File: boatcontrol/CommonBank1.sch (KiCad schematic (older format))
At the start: 21 parts, among them J201 Conn_01x01_Male, J202 Conn_01x01_Male, J203 TBP01R2W-508-16BE, J204 Conn_01x01_Male, J205 Conn_01x01_Male, J206 TBL008V-1000-02BE, Q203 IRF9510PBF-BE3, U201 MCP23017-E/SP, U202 MCP23017-E/SP

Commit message: Try labels on subcharts
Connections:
- net labels added: 12C_RAW
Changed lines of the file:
@@
 L power:+12C #PWR?
 U 1 1 D1AAA2AE
-P 9000 6050
+P 8100 6050
 AR Path="/D1AAA2AE" Ref="#PWR?"  Part="1"
 AR Path="/D16552B4/D1AAA2AE" Ref="#PWR0205"  Part="1"
 AR Path="/D1BB8DB4/D1AAA2AE" Ref="#PWR?"  Part="1"
-F 0 "#PWR0205" H 9000 5900 50  0001 C CNN
-F 1 "+12C" H 8950 6200 50  0000 L CNN
-F 2 "" H 9000 6050 50  0001 C CNN
-F 3 "" H 9000 6050 50  0001 C CNN
-	1    9000 6050
+F 0 "#PWR0205" H 8100 5900 50  0001 C CNN
+F 1 "+12C" H 8050 6200 50  0000 L CNN
+F 2 "" H 8100 6050 50  0001 C CNN
+F 3 "" H 8100 6050 50  0001 C CNN
+	1    8100 6050
 	1    0    0    -1
 $EndComp
@@
 Wire Wire Line
 	6700 4600 7550 4600
-Wire Wire Line
-	9250 6050 9000 6050
 Wire Wire Line
 	6750 1050 6700 1050
@@
 L power:PWR_FLAG #FLG0201
 U 1 1 5F1AB3C0
-P 9250 6050
-F 0 "#FLG0201" H 9250 6125 50  0001 C CNN
-F 1 "PWR_FLAG" H 9250 6223 50  0000 C CNN
-F 2 "" H 9250 6050 50  0001 C CNN
-F 3 "~" H 9250 6050 50  0001 C CNN
-	1    9250 6050
+P 8100 6050
+F 0 "#FLG0201" H 8100 6125 50  0001 C CNN
+F 1 "PWR_FLAG" H 8100 6223 50  0000 C CNN
+F 2 "" H 8100 6050 50  0001 C CNN
+F 3 "~" H 8100 6050 50  0001 C CNN
+	1    8100 6050
 	-1   0    0    1
 $EndComp
-Connection ~ 9250 6050
 Text Notes 3300 2100 3    50   ~ 0
 I2C Address 0x20
@@
 	6750 5250 6750 6050
 Wire Wire Line
-	8300 6050 6750 6050
+	8300 6050 8100 6050
 Connection ~ 6750 6050
 Wire Wire Line
 	6750 6050 6750 6250
-Wire Wire Line
-	8700 6050 9000 6050
-Connection ~ 9000 6050
 $Comp
 L power:GND #PWR0204
@@
 Wire Wire Line
 	8500 5750 8800 5750
+Text Label 9150 6050 2    50   ~ 0
+12C_RAW
+Wire Wire Line
+	8700 6050 9250 6050
+Connection ~ 8100 6050
+Wire Wire Line
+	6750 6050 8100 6050
 $EndSCHEMATC

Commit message: Bottom done
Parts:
- removed Q203: IRF9510PBF-BE3, Package_TO_SOT_THT:TO-220-3_Vertical, symbol BoatControl:IPP_B_I80P03
- added Q203: IPP120P04P4L-03, Package_TO_SOT_THT:TO-220-3_Vertical, symbol BoatControl:IPP120P04P4L-03
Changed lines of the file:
@@
 Wire Wire Line
 	1100 7150 1700 7150
-$Comp
-L BoatControl:IPP_B_I80P03 Q?
-U 1 1 6232FD99
-P 8500 6050
-AR Path="/6232FD99" Ref="Q?"  Part="1"
-AR Path="/D16552B4/6232FD99" Ref="Q203"  Part="1"
-F 0 "Q203" V 8350 5850 50  0000 L CNN
-F 1 "IRF9510PBF-BE3" V 8750 5850 50  0000 L CNN
-F 2 "Package_TO_SOT_THT:TO-220-3_Vertical" H 8500 6050 50  0001 C CNN
-F 3 "https://www.vishay.com/docs/91072/91072.pdf" H 8500 6050 50  0001 C CNN
-F 4 "P-Channel 100V 4A (Tc) 43W (Tc) Through Hole TO-220AB" H 8500 6050 50  0001 C CNN "Description"
-F 5 "Vishay Siliconix" H 8500 6050 50  0001 C CNN "Manufacturer"
-	1    8500 6050
-	0    1    1    0
-$EndComp
 Wire Wire Line
 	6750 5250 6750 6050
@@
 Wire Wire Line
 	6750 6050 8100 6050
+$Comp
+L BoatControl:IPP120P04P4L-03 Q203
+U 1 1 5FEBFE7C
+P 8500 6050
+F 0 "Q203" V 8150 6050 50  0000 C CNN
+F 1 "IPP120P04P4L-03" V 8650 6250 50  0000 C CNN
+F 2 "Package_TO_SOT_THT:TO-220-3_Vertical" H 8150 6600 50  0001 C CNN
+F 3 "https://www.infineon.com/dgdl/Infineon-I80P03P4L_04-DS-v01_01-en.pdf?folderId=db3a304314dca3890114ef902baa05f9&fileId=db3a30431ddc9372011e07e95eb827d7&ack=t" H 8500 6050 50  0001 C CNN
+F 4 "P-Channel 30V 80A (Tc) 137W (Tc) Through Hole PG-TO220-3-1" H 8350 6700 50  0001 C CNN "Description"
+F 5 "OptiMOS" H 9100 6350 50  0001 C CNN "Series"
+F 6 "Infineon Technologies" H 9000 6450 50  0001 C CNN "Infineon Technologies"
+	1    8500 6050
+	0    1    1    0
+$EndComp
 $EndSCHEMATC

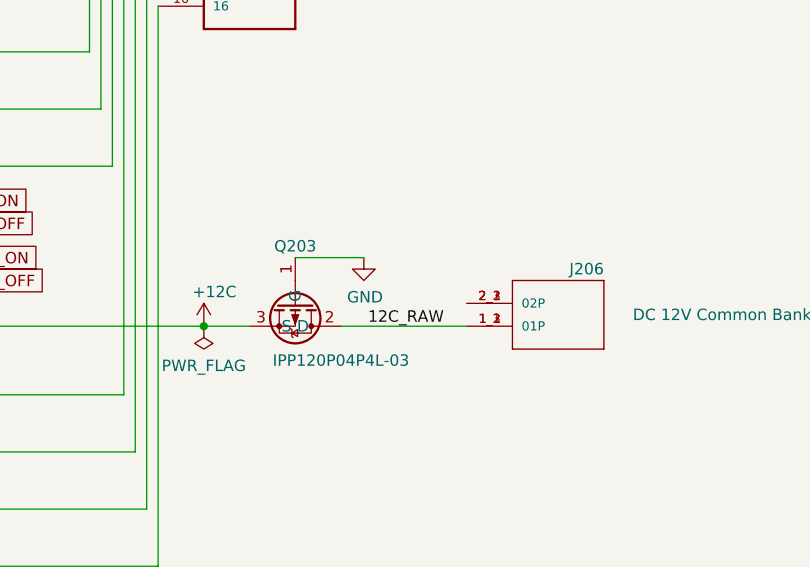
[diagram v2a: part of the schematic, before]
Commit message: Fix polarity mosfets
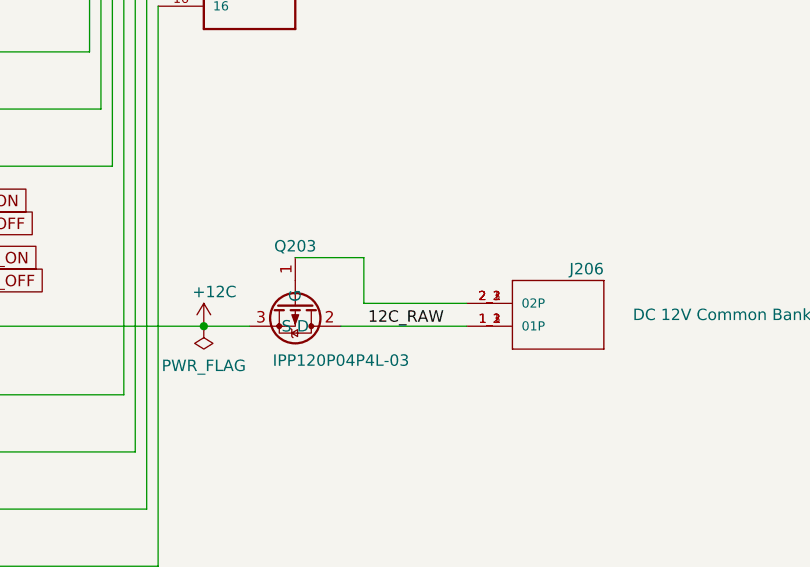
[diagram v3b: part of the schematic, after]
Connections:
- net GND: no longer Q203.1 (G)
- net at J206.2_1 (02P), J206.2_2 (02P), J206.2_3 (02P): now also Q203.1 (G)
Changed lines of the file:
@@
 Wire Wire Line
 	6750 6050 6750 6250
-$Comp
-L power:GND #PWR0204
-U 1 1 623B0B10
-P 8800 5750
-F 0 "#PWR0204" H 8800 5500 50  0001 C CNN
-F 1 "GND" H 8805 5577 50  0000 C CNN
-F 2 "" H 8800 5750 50  0001 C CNN
-F 3 "" H 8800 5750 50  0001 C CNN
-	1    8800 5750
-	1    0    0    -1
-$EndComp
 Wire Wire Line
 	4600 1650 5400 1650
@@
 	0    1    1    0
 $EndComp
+Wire Wire Line
+	9250 5950 8800 5950
+Wire Wire Line
+	8800 5950 8800 5750
 $EndSCHEMATC

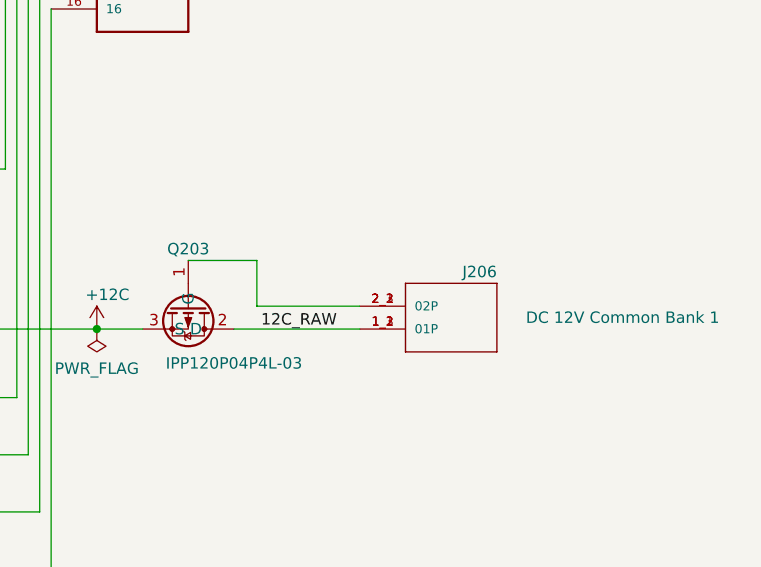
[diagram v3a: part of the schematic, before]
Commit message: Add reverse/AC/DC polarity indicators
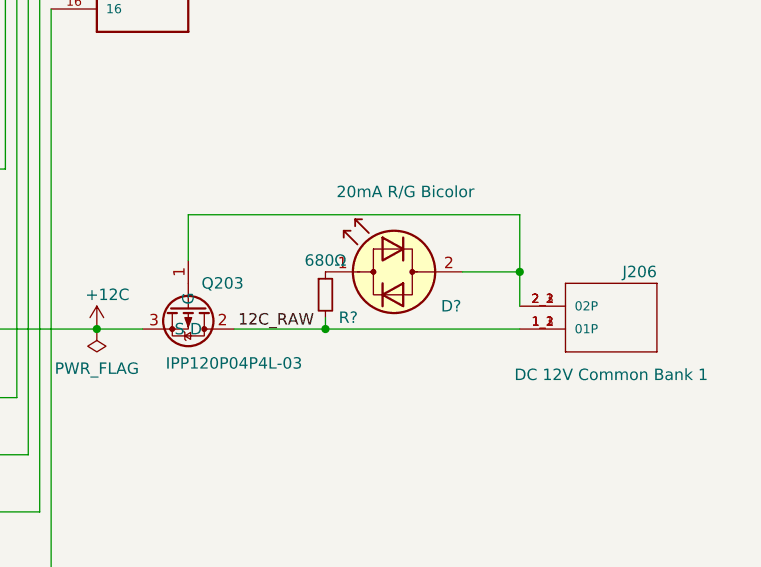
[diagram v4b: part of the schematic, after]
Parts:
- added D?: 20mA R/G Bicolor, LED_THT:LED_D5.0mm, symbol Device:LED_Dual_2pin
- added R?: 680Ω, Resistor_THT:R_Axial_DIN0207_L6.3mm_D2.5mm_P7.62mm_Horizontal, symbol Device:R_Small
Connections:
- net 12C_RAW: now also R?.2
- net at J206.2_1 (02P), J206.2_2 (02P), J206.2_3 (02P)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: now also D?.2 (AK)
- new net: D?.1 (KA), R?.1
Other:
- moved on the sheet: J206

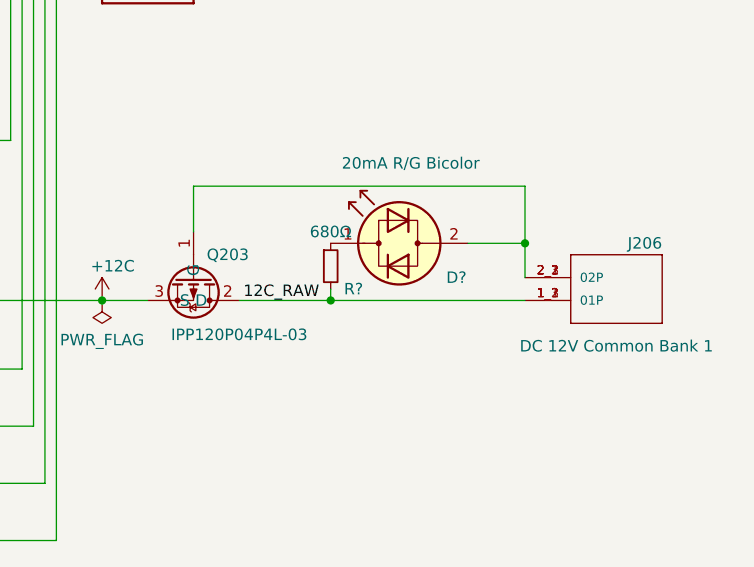
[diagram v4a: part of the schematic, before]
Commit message: Fix LED resistors
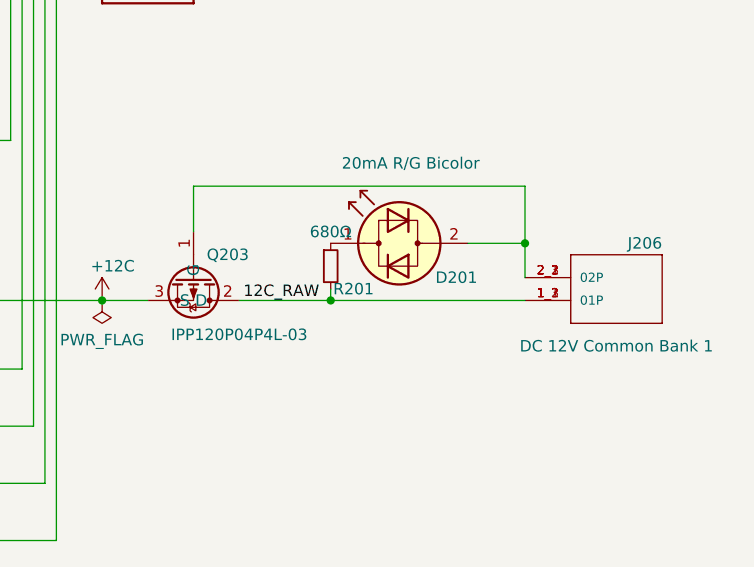
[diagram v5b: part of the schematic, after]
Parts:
- gave numbers to parts that had none: 2
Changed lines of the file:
@@
 AR Path="/D1BB8DB4/5F75E923/60474907/5FECB36F" Ref="D?"  Part="1"
 AR Path="/D1BB8DB4/5F75E923/60474911/5FECB36F" Ref="D?"  Part="1"
-AR Path="/D16552B4/5FECB36F" Ref="D?"  Part="1"
-F 0 "D?" H 9150 5650 50  0000 C CNN
+AR Path="/D16552B4/5FECB36F" Ref="D201"  Part="1"
+F 0 "D201" H 9150 5650 50  0000 C CNN
 F 1 "20mA R/G Bicolor" H 9350 6150 50  0000 C CNN
 F 2 "LED_THT:LED_D5.0mm" H 9400 5800 50  0001 C CNN
@@
 $EndComp
 $Comp
-L Device:R_Small R?
+L Device:R_Small R201
 U 1 1 5FE96CCA
 P 9100 5900
-F 0 "R?" H 9200 5800 50  0000 C CNN
+F 0 "R201" H 9200 5800 50  0000 C CNN
 F 1 "680Ω" H 9100 6050 50  0000 C CNN
 F 2 "Resistor_THT:R_Axial_DIN0207_L6.3mm_D2.5mm_P7.62mm_Horizontal" H 9100 5900 50  0001 C CNN

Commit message: Figure out wiring cluster
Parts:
- added JP209: Jumper_NO_Small, Connector_PinHeader_2.54mm:PinHeader_1x02_P2.54mm_Vertical, symbol Device:Jumper_NO_Small
- Q203: Field8 (none) -> Optional, can be substituded with shunt; Purpose (none) -> Reverse Polarity (Voltage) Protection
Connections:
- net at J206.2_1 (02P), J206.2_2 (02P), J206.2_3 (02P)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: now also JP209.1; no longer D201.2 (AK)
- new net: D201.2 (AK), JP209.2
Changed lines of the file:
@@
 F 5 "OptiMOS" H 9100 6350 50  0001 C CNN "Series"
 F 6 "Infineon Technologies" H 9000 6450 50  0001 C CNN "Infineon Technologies"
+F 7 "Reverse Polarity (Voltage) Protection" V 8800 6200 50  0000 C CNN "Purpose"
+F 8 "Optional, can be substituded with shunt" V 8900 6250 50  0000 C CNN "Field8"
 	1    8500 6050
 	0    1    1    0
@@
 Wire Wire Line
 	8500 5550 8500 5750
+$Comp
+L Device:Jumper_NO_Small JP?
+U 1 1 617F409D
+P 9800 5800
+AR Path="/617F409D" Ref="JP?"  Part="1"
+AR Path="/D16552B4/617F409D" Ref="JP209"  Part="1"
+AR Path="/D1BB8DB4/617F409D" Ref="JP?"  Part="1"
+F 0 "JP209" H 9800 5900 50  0000 C CNN
+F 1 "Jumper_NO_Small" H 9850 5700 50  0001 C CNN
+F 2 "Connector_PinHeader_2.54mm:PinHeader_1x02_P2.54mm_Vertical" H 9800 5800 50  0001 C CNN
+F 3 "~" H 9800 5800 50  0001 C CNN
+	1    9800 5800
+	-1   0    0    1
+$EndComp
 Wire Wire Line
-	9950 5800 9950 5550
+	9950 5550 9950 5800
 Wire Wire Line
-	9950 5950 9950 5800
+	9900 5800 9950 5800
 Connection ~ 9950 5800
 Wire Wire Line
-	9950 5800 9700 5800
+	9950 5800 9950 5950
 $EndSCHEMATC

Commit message: Add remaining bypass capacitors
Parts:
- C201, C203: value 10uF -> 10μF; footprint Capacitor_THT:CP_Radial_D8.0mm_P5.00mm -> Capacitor_THT:C_Disc_D7.5mm_W5.0mm_P5.00mm; symbol Device:CP1_Small -> Device:C_Small
- C202, C204: value 0.1uF -> 0.1μF; footprint Capacitor_THT:CP_Radial_D8.0mm_P5.00mm -> Capacitor_THT:C_Disc_D7.5mm_W5.0mm_P5.00mm; symbol Device:CP1_Small -> Device:C_Small
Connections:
- net 12V DC Block 3/DIG_OFF_C1: no longer U202.2 (GPB1)
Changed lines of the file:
@@
 	2350 6150 2350 4950
 Wire Wire Line
-	2350 4950 3550 4950
+	2350 4950 3200 4950
 Connection ~ 2350 6150
 Wire Wire Line
@@
 Wire Wire Line
 	2350 2000 2350 800
-Wire Wire Line
-	2350 800  3550 800
 Connection ~ 2350 2000
 Wire Wire Line
@@
 AR Path="/D1BB8DB4/5FA17E9C" Ref="#PWR?"  Part="1"
 F 0 "#PWR0203" H 3550 4800 50  0001 C CNN
-F 1 "+5V" H 3700 5000 50  0000 C CNN
+F 1 "+5V" V 3550 5150 50  0000 C CNN
 F 2 "" H 3550 4950 50  0001 C CNN
 F 3 "" H 3550 4950 50  0001 C CNN
 	1    3550 4950
-	1    0    0    -1
+	0    1    1    0
 $EndComp
 Connection ~ 3550 800
@@
 AR Path="/D1BB8DB4/5FA17EB1" Ref="#PWR?"  Part="1"
 F 0 "#PWR0201" H 3550 650 50  0001 C CNN
-F 1 "+5V" H 3700 850 50  0000 C CNN
+F 1 "+5V" V 3550 1000 50  0000 C CNN
 F 2 "" H 3550 800 50  0001 C CNN
 F 3 "" H 3550 800 50  0001 C CNN
 	1    3550 800
-	1    0    0    -1
+	0    1    1    0
 $EndComp
 Connection ~ 3550 3000
@@
 Wire Wire Line
 	5400 4600 4300 4600
-Wire Wire Line
-	4300 4600 4300 5350
 Wire Wire Line
 	5400 4750 4350 4750
@@
 	6750 6250 6750 6500
 $Comp
-L Device:CP1_Small C?
-U 1 1 61835D4A
-P 900 1800
-AR Path="/61835D4A" Ref="C?"  Part="1"
-AR Path="/D16552B4/61835D4A" Ref="C201"  Part="1"
-F 0 "C201" V 850 1550 50  0000 L CNN
-F 1 "10uF" H 991 1755 50  0001 L CNN
-F 2 "Capacitor_THT:CP_Radial_D8.0mm_P5.00mm" H 900 1800 50  0001 C CNN
-F 3 "https://www.mouser.ca/datasheet/2/212/KEM_C1050_GOLDMAX_X7R-1518817.pdf" H 900 1800 50  0001 C CNN
-F 4 "Kemet" H 900 1800 50  0001 C CNN "Manufacturer"
-F 5 "C322C106K3R5TA" V 900 1800 50  0001 C CNN "Model"
-	1    900  1800
-	1    0    0    -1
-$EndComp
-$Comp
-L Device:CP1_Small C?
+L Device:C_Small C?
 U 1 1 61835D52
-P 1100 1800
+P 3450 700
 AR Path="/61835D52" Ref="C?"  Part="1"
 AR Path="/D16552B4/61835D52" Ref="C202"  Part="1"
-F 0 "C202" V 1050 1550 50  0000 L CNN
-F 1 "0.1uF" H 1191 1755 50  0001 L CNN
-F 2 "Capacitor_THT:CP_Radial_D8.0mm_P5.00mm" H 1100 1800 50  0001 C CNN
-F 3 "https://www.mouser.ca/datasheet/2/212/KEM_C1050_GOLDMAX_X7R-1518817.pdf" H 1100 1800 50  0001 C CNN
-F 4 "Kemet" H 1100 1800 50  0001 C CNN "Manufacturer"
-F 5 "C320C104K3R5TA" V 1100 1800 50  0001 C CNN "Model"
-	1    1100 1800
-	1    0    0    -1
-$EndComp
-Wire Wire Line
-	900  1700 900  800
-Wire Wire Line
-	1100 800  1100 1700
-Wire Wire Line
-	900  1900 900  3000
-Wire Wire Line
-	1100 1900 1100 3000
-$Comp
-L Device:CP1_Small C?
+F 0 "C202" H 3350 900 50  0000 L CNN
+F 1 "0.1μF" H 3541 655 50  0001 L CNN
+F 2 "Capacitor_THT:C_Disc_D7.5mm_W5.0mm_P5.00mm" H 3450 700 50  0001 C CNN
+F 3 "https://www.mouser.ca/datasheet/2/212/KEM_C1050_GOLDMAX_X7R-1518817.pdf" H 3450 700 50  0001 C CNN
+F 4 "Kemet" H 3450 700 50  0001 C CNN "Manufacturer"
+F 5 "C320C104K3R5TA" V 3450 700 50  0001 C CNN "Model"
+	1    3450 700
+	-1   0    0    1
+$EndComp
+$Comp
+L Device:C_Small C?
 U 1 1 61844324
-P 900 5950
+P 3200 4850
 AR Path="/61844324" Ref="C?"  Part="1"
 AR Path="/D16552B4/61844324" Ref="C203"  Part="1"
-F 0 "C203" V 850 5700 50  0000 L CNN
-F 1 "10uF" H 991 5905 50  0001 L CNN
-F 2 "Capacitor_THT:CP_Radial_D8.0mm_P5.00mm" H 900 5950 50  0001 C CNN
-F 3 "https://www.mouser.ca/datasheet/2/212/KEM_C1050_GOLDMAX_X7R-1518817.pdf" H 900 5950 50  0001 C CNN
-F 4 "Kemet" H 900 5950 50  0001 C CNN "Manufacturer"
-F 5 "C322C106K3R5TA" V 900 5950 50  0001 C CNN "Model"
-	1    900  5950
-	1    0    0    -1
-$EndComp
-$Comp
-L Device:CP1_Small C?
+F 0 "C203" H 3100 4650 50  0000 L CNN
+F 1 "10μF" H 3291 4805 50  0001 L CNN
+F 2 "Capacitor_THT:C_Disc_D7.5mm_W5.0mm_P5.00mm" H 3200 4850 50  0001 C CNN
+F 3 "https://www.mouser.ca/datasheet/2/212/KEM_C1050_GOLDMAX_X7R-1518817.pdf" H 3200 4850 50  0001 C CNN
+F 4 "Kemet" H 3200 4850 50  0001 C CNN "Manufacturer"
+F 5 "C322C106K3R5TA" V 3200 4850 50  0001 C CNN "Model"
+	1    3200 4850
+	-1   0    0    1
+$EndComp
+$Comp
+L Device:C_Small C?
 U 1 1 6184432C
-P 1100 5950
+P 3450 4850
 AR Path="/6184432C" Ref="C?"  Part="1"
 AR Path="/D16552B4/6184432C" Ref="C204"  Part="1"
-F 0 "C204" V 1050 5700 50  0000 L CNN
-F 1 "0.1uF" H 1191 5905 50  0001 L CNN
-F 2 "Capacitor_THT:CP_Radial_D8.0mm_P5.00mm" H 1100 5950 50  0001 C CNN
-F 3 "https://www.mouser.ca/datasheet/2/212/KEM_C1050_GOLDMAX_X7R-1518817.pdf" H 1100 5950 50  0001 C CNN
-F 4 "Kemet" H 1100 5950 50  0001 C CNN "Manufacturer"
-F 5 "C320C104K3R5TA" V 1100 5950 50  0001 C CNN "Model"
-	1    1100 5950
-	1    0    0    -1
-$EndComp
-Wire Wire Line
-	900  5850 900  4950
-Wire Wire Line
-	1100 4950 1100 5850
-Wire Wire Line
-	900  6050 900  7150
-Wire Wire Line
-	1100 6050 1100 7150
-Wire Wire Line
-	900  800  1100 800
-Connection ~ 1300 800
-Connection ~ 1100 800
-Wire Wire Line
-	1100 800  1300 800
-Wire Wire Line
-	900  3000 1100 3000
-Connection ~ 1700 3000
-Connection ~ 1100 3000
-Wire Wire Line
-	1100 3000 1700 3000
-Wire Wire Line
-	900  4950 1100 4950
-Connection ~ 1300 4950
-Connection ~ 1100 4950
-Wire Wire Line
-	1100 4950 1300 4950
-Wire Wire Line
-	900  7150 1100 7150
-Connection ~ 1700 7150
-Connection ~ 1100 7150
-Wire Wire Line
-	1100 7150 1700 7150
+F 0 "C204" H 3350 4650 50  0000 L CNN
+F 1 "0.1μF" H 3541 4805 50  0001 L CNN
+F 2 "Capacitor_THT:C_Disc_D7.5mm_W5.0mm_P5.00mm" H 3450 4850 50  0001 C CNN
+F 3 "https://www.mouser.ca/datasheet/2/212/KEM_C1050_GOLDMAX_X7R-1518817.pdf" H 3450 4850 50  0001 C CNN
+F 4 "Kemet" H 3450 4850 50  0001 C CNN "Manufacturer"
+F 5 "C320C104K3R5TA" V 3450 4850 50  0001 C CNN "Model"
+	1    3450 4850
+	-1   0    0    1
+$EndComp
 Wire Wire Line
 	6750 5250 6750 6050
@@
 Wire Wire Line
 	9950 5800 9950 5950
+Wire Wire Line
+	3200 600  3450 600
+$Comp
+L power:GND #PWR0189
+U 1 1 61DD4C34
+P 3450 600
+F 0 "#PWR0189" H 3450 350 50  0001 C CNN
+F 1 "GND" V 3455 472 50  0000 R CNN
+F 2 "" H 3450 600 50  0001 C CNN
+F 3 "" H 3450 600 50  0001 C CNN
+	1    3450 600
+	0    -1   -1   0
+$EndComp
+Connection ~ 3450 800
+Wire Wire Line
+	3450 800  3550 800
+Connection ~ 3450 600
+Connection ~ 3200 4950
+Wire Wire Line
+	3200 4950 3450 4950
+Connection ~ 3450 4950
+Wire Wire Line
+	3450 4950 3550 4950
+Wire Wire Line
+	3200 4750 3450 4750
+$Comp
+L power:GND #PWR0190
+U 1 1 61E66AA4
+P 3450 4750
+F 0 "#PWR0190" H 3450 4500 50  0001 C CNN
+F 1 "GND" V 3455 4622 50  0000 R CNN
+F 2 "" H 3450 4750 50  0001 C CNN
+F 3 "" H 3450 4750 50  0001 C CNN
+	1    3450 4750
+	0    -1   -1   0
+$EndComp
+Connection ~ 3450 4750
+Connection ~ 3200 800
+Wire Wire Line
+	3200 800  3450 800
+Wire Wire Line
+	2350 800  3200 800
+$Comp
+L Device:C_Small C?
+U 1 1 61835D4A
+P 3200 700
+AR Path="/61835D4A" Ref="C?"  Part="1"
+AR Path="/D16552B4/61835D4A" Ref="C201"  Part="1"
+F 0 "C201" H 3100 900 50  0000 L CNN
+F 1 "10μF" H 3291 655 50  0001 L CNN
+F 2 "Capacitor_THT:C_Disc_D7.5mm_W5.0mm_P5.00mm" H 3200 700 50  0001 C CNN
+F 3 "https://www.mouser.ca/datasheet/2/212/KEM_C1050_GOLDMAX_X7R-1518817.pdf" H 3200 700 50  0001 C CNN
+F 4 "Kemet" H 3200 700 50  0001 C CNN "Manufacturer"
+F 5 "C322C106K3R5TA" V 3200 700 50  0001 C CNN "Model"
+	1    3200 700
+	-1   0    0    1
+$EndComp
 $EndSCHEMATC
